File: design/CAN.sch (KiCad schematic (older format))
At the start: 4 parts, among them U401 SN65HVD232

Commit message: Added PDF schematic
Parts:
- C401: footprint SMD_Packages:SMD-0603 -> SMD_Packages:SMD-0402
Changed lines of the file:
@@
 F 0 "C401" H 6150 3500 40  0000 L CNN
 F 1 "100nF" H 6156 3315 40  0000 L CNN
-F 2 "SMD_Packages:SMD-0603" H 6188 3250 30  0001 C CNN
+F 2 "SMD_Packages:SMD-0402" H 6188 3250 30  0001 C CNN
 F 3 "" H 6150 3400 60  0000 C CNN
 	1    6150 3400

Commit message: Changed some component values
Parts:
- C401: value 100nF -> 1u
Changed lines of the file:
@@
 P 6150 3400
 F 0 "C401" H 6150 3500 40  0000 L CNN
-F 1 "100nF" H 6156 3315 40  0000 L CNN
+F 1 "1u" H 6156 3315 40  0000 L CNN
 F 2 "SMD_Packages:SMD-0402" H 6188 3250 30  0001 C CNN
 F 3 "" H 6150 3400 60  0000 C CNN

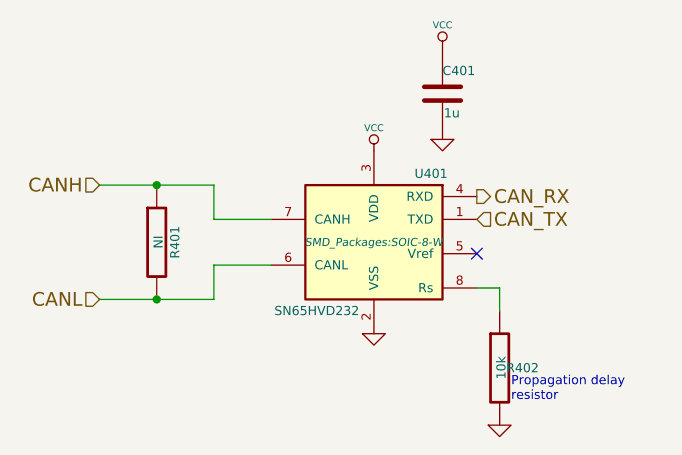
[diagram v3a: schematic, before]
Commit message: Moved nRST cap closer to the MCU pin, connected crystal GND pins to the actual GND plane. Added several vias to GND and VDD planes.
Signed-off-by: Marcos Chaparro <marcos@mrkindustries.com.ar>
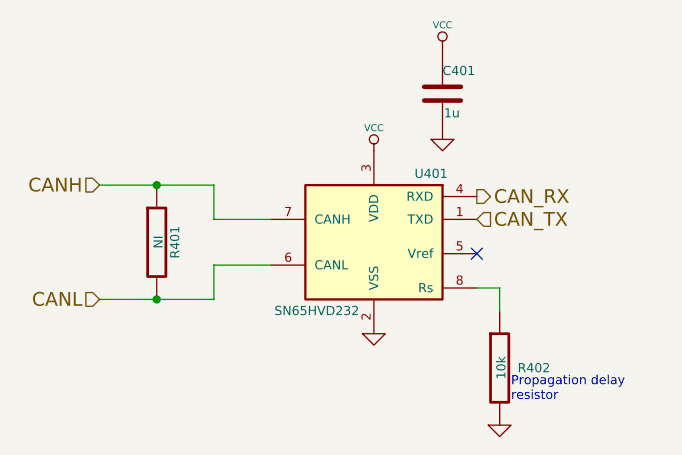
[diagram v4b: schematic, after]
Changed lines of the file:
@@
 F 0 "U401" H 5600 4350 40  0000 C CNN
 F 1 "SN65HVD232" H 6100 3750 40  0000 C CNN
-F 2 "SMD_Packages:SOIC-8-W" H 5850 4050 35  0000 C CIN
+F 2 "SMD_Packages:SOIC-8-W" H 5850 4050 35  0001 C CIN
 F 3 "" H 5850 4050 60  0000 C CNN
 	1    5850 4050
@@
 $EndComp
 $Comp
-L GND #PWR029
+L GND #PWR028
 U 1 1 53F59F97
 P 5850 4450
-F 0 "#PWR029" H 5850 4450 30  0001 C CNN
+F 0 "#PWR028" H 5850 4450 30  0001 C CNN
 F 1 "GND" H 5850 4380 30  0001 C CNN
 F 2 "" H 5850 4450 60  0000 C CNN
@@
 $EndComp
 $Comp
-L VCC #PWR030
+L VCC #PWR029
 U 1 1 53F59F9D
 P 5850 3650
-F 0 "#PWR030" H 5850 3750 30  0001 C CNN
+F 0 "#PWR029" H 5850 3750 30  0001 C CNN
 F 1 "VCC" H 5850 3750 30  0000 C CNN
 F 2 "" H 5850 3650 60  0001 C CNN
@@
 $EndComp
 $Comp
-L VCC #PWR031
+L VCC #PWR030
 U 1 1 53F59FAA
 P 6150 3200
-F 0 "#PWR031" H 6150 3300 30  0001 C CNN
+F 0 "#PWR030" H 6150 3300 30  0001 C CNN
 F 1 "VCC" H 6150 3300 30  0000 C CNN
 F 2 "" H 6150 3200 60  0001 C CNN
@@
 $EndComp
 $Comp
-L GND #PWR032
+L GND #PWR031
 U 1 1 53F59FB0
 P 6150 3600
-F 0 "#PWR032" H 6150 3600 30  0001 C CNN
+F 0 "#PWR031" H 6150 3600 30  0001 C CNN
 F 1 "GND" H 6150 3530 30  0001 C CNN
 F 2 "" H 6150 3600 60  0000 C CNN
@@
 $Bitmap
 Pos 8850 4800
-Scale 1,000000
+Scale 1.000000
 Data
 89 50 4E 47 0D 0A 1A 0A 00 00 00 0D 49 48 44 52 00 00 01 8D 00 00 01 8C 08 02 00 00 00 A9 99 69
@@
 U 1 1 54003136
 P 6400 4600
-F 0 "R402" H 6500 4600 40  0000 C CNN
+F 0 "R402" H 6550 4600 40  0000 C CNN
 F 1 "10k" V 6407 4601 40  0000 C CNN
 F 2 "SMD_Packages:SMD-0603_r" V 6330 4600 30  0001 C CNN
@@
 	6400 4250 6300 4250
 $Comp
-L GND #PWR033
+L GND #PWR032
 U 1 1 5400318B
 P 6400 4850
-F 0 "#PWR033" H 6400 4850 30  0001 C CNN
+F 0 "#PWR032" H 6400 4850 30  0001 C CNN
 F 1 "GND" H 6400 4780 30  0001 C CNN
 F 2 "" H 6400 4850 60  0000 C CNN

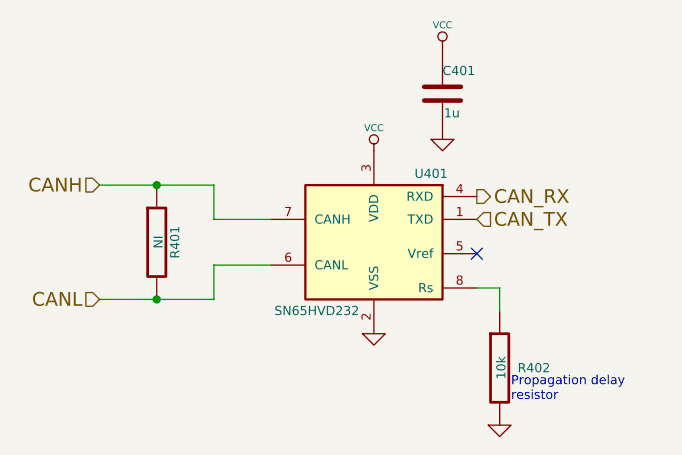
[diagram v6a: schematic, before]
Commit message: Changed some capacitor values, made new assembly PDFs, added comment about R16 to schematic
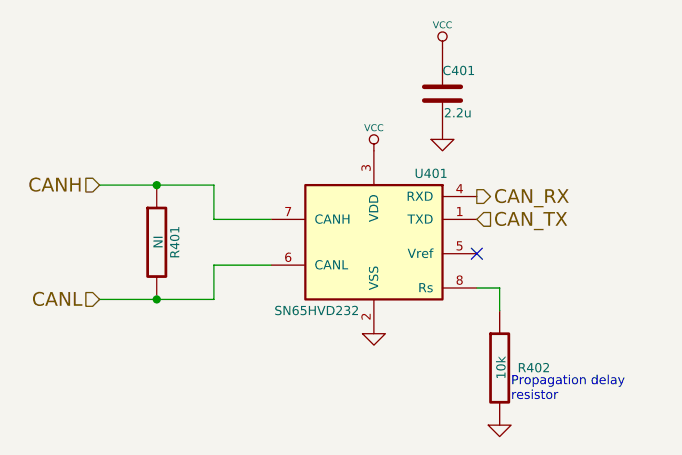
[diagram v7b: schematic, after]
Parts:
- C401: value 1u -> 2.2u
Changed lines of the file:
@@
 P 6150 3400
 F 0 "C401" H 6150 3500 40  0000 L CNN
-F 1 "1u" H 6156 3315 40  0000 L CNN
+F 1 "2.2u" H 6156 3315 40  0000 L CNN
 F 2 "SMD_Packages:SMD-0402" H 6188 3250 30  0001 C CNN
 F 3 "" H 6150 3400 60  0000 C CNN
